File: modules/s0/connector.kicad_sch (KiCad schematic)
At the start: 15 parts, among them J1 P8, J2 P9, J3 USB_C_Receptacle_USB2.0_14P, J4 BAT_JST_01x02, U2 LM2575S-3.3(UMW), U4 BEAGLEBONEBLACK

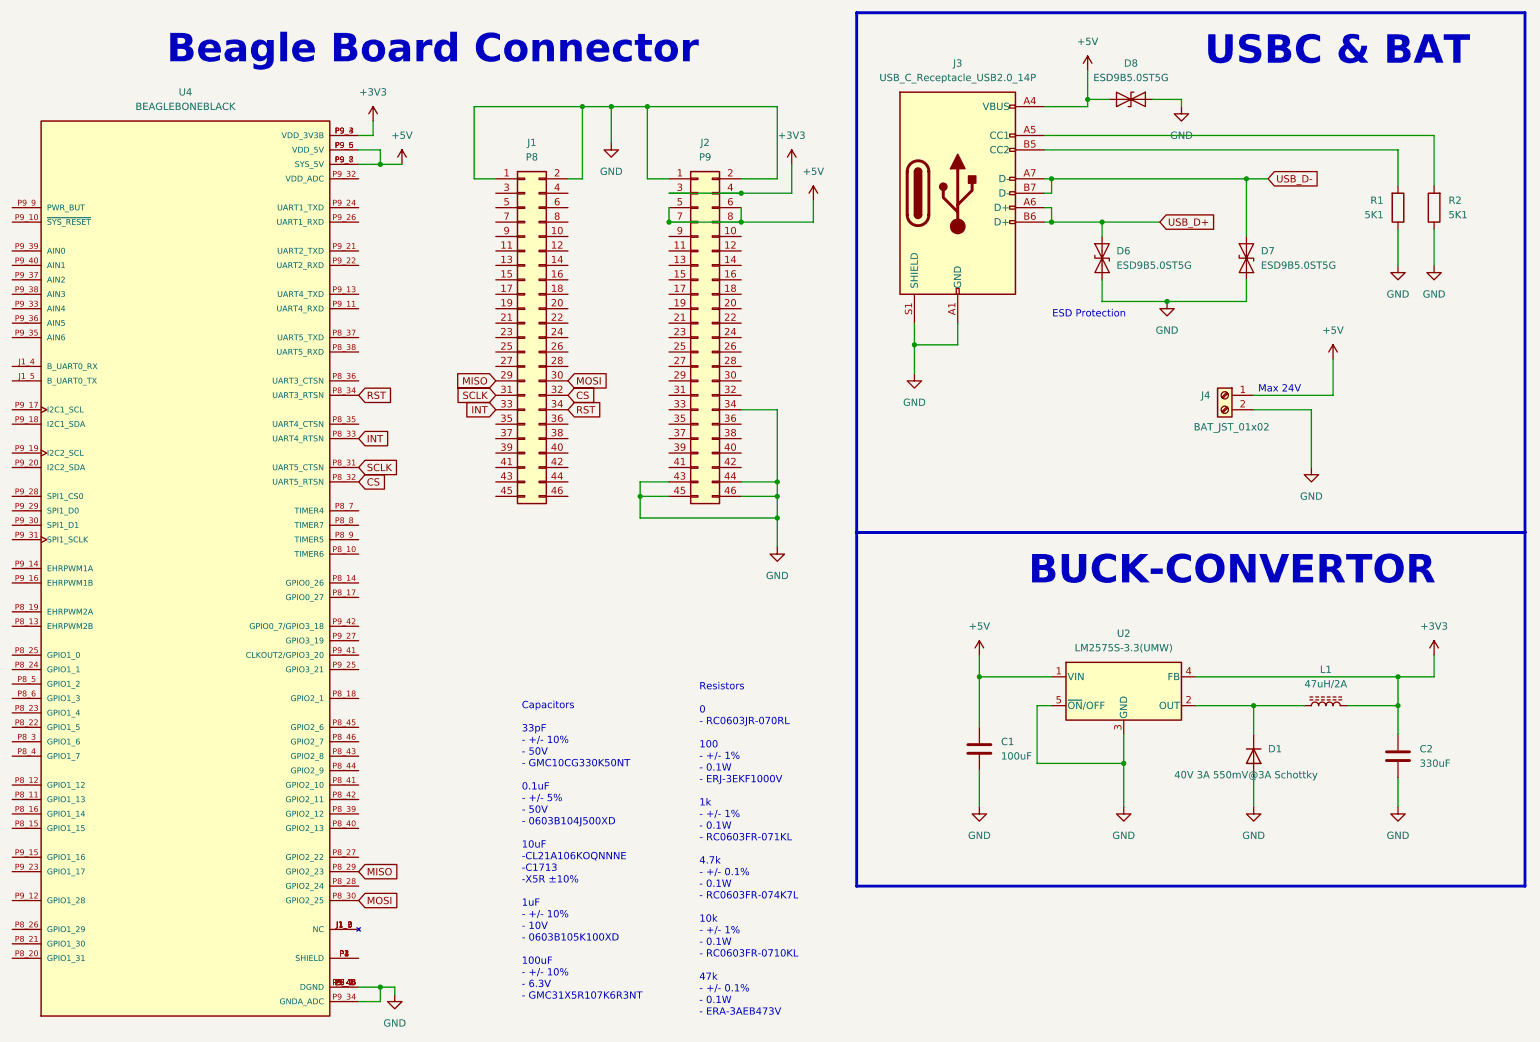
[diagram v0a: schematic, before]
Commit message: fix: add fuse, ferrite bead and fixes from gpt
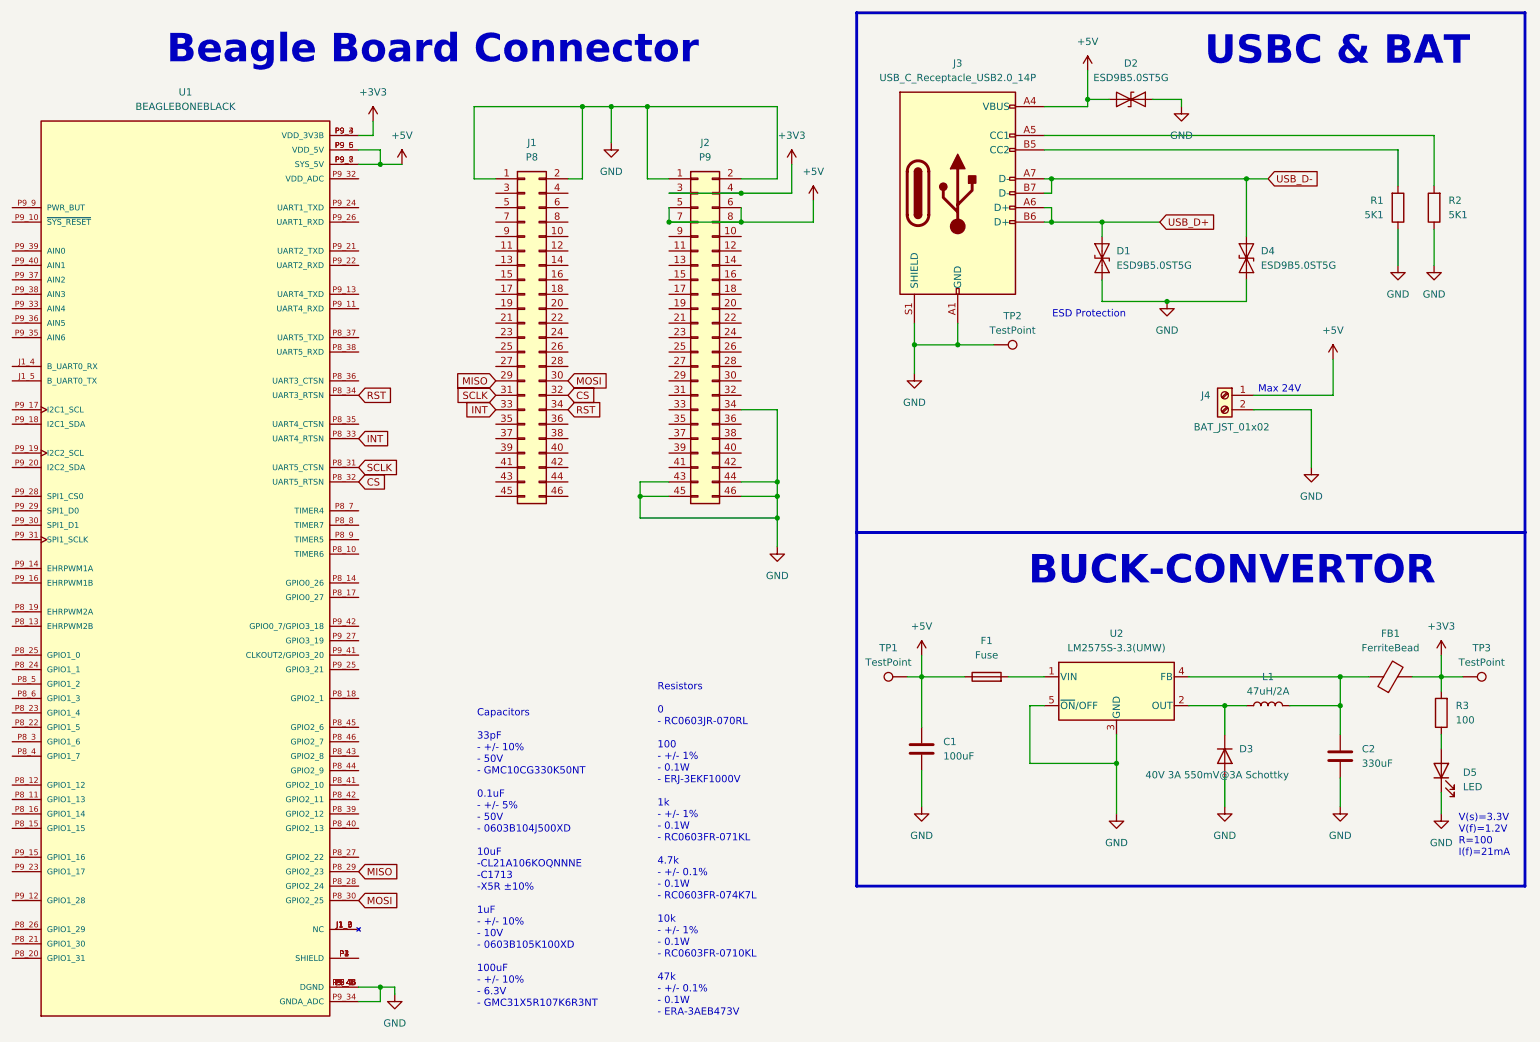
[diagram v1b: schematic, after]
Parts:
- added D5: LED, LED_SMD:LED_0603_1608Metric, symbol Device:LED
- added F1: Fuse, Fuse:Fuse_1206_3216Metric_Pad1.42x1.75mm_HandSolder, symbol Device:Fuse
- added FB1: FerriteBead, Inductor_SMD:L_1206_3216Metric_Pad1.22x1.90mm_HandSolder, symbol Device:FerriteBead
- added R3: 100, Resistor_SMD:R_0402_1005Metric, symbol Device:R
- added TP1, TP2, TP3: TestPoint, TestPoint:TestPoint_Pad_D1.0mm, symbol Connector:TestPoint
- L1: symbol Device:L_Ferrite -> Device:L
- renumbered D6 to D1, D8 to D2, D1 to D3, D7 to D4, U4 to U1
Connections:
- net +3V3: now also FB1.2, R3.2, TP3.1; no longer C2.1, L1.2, U2.4 (FB)
- net +5V: now also F1.1, TP1.1; no longer U2.1 (VIN)
- net GND: now also D5.1 (K), TP2.1
- new net: C2.1, FB1.1, L1.2, U2.4 (FB)
- new net: F1.2, U2.1 (VIN)
- new net: D5.2 (A), R3.1
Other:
- note added: "V(s)=3.3V V(f)=1.2V R=100 I(f)=21mA"
- moved on the sheet: C1, C2, D3, U2

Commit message: chore: finalize production files for s0
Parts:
- C1: value 100uF -> 10uF
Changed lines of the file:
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@@
 			)
 		)
-		(property "Value" "100uF"
+		(property "Value" "10uF"
 			(at 182.88 143.5099 0)
 			(effects

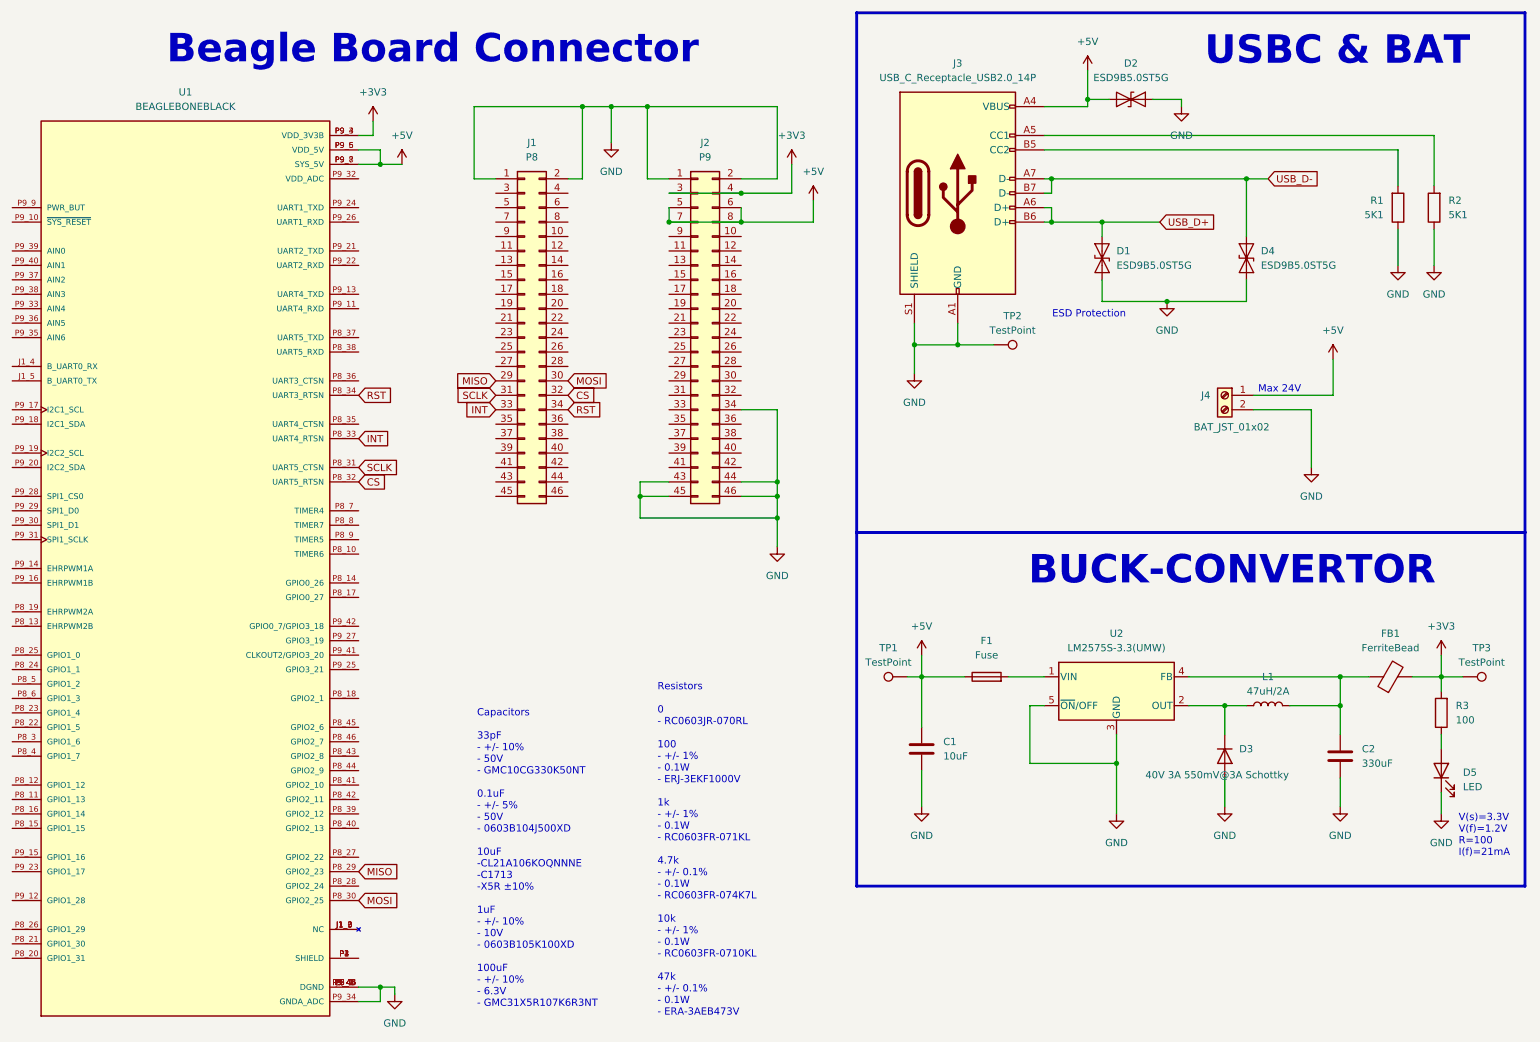
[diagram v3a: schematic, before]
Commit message: feat(s0): add GPIO mux for wired mbus and sd card
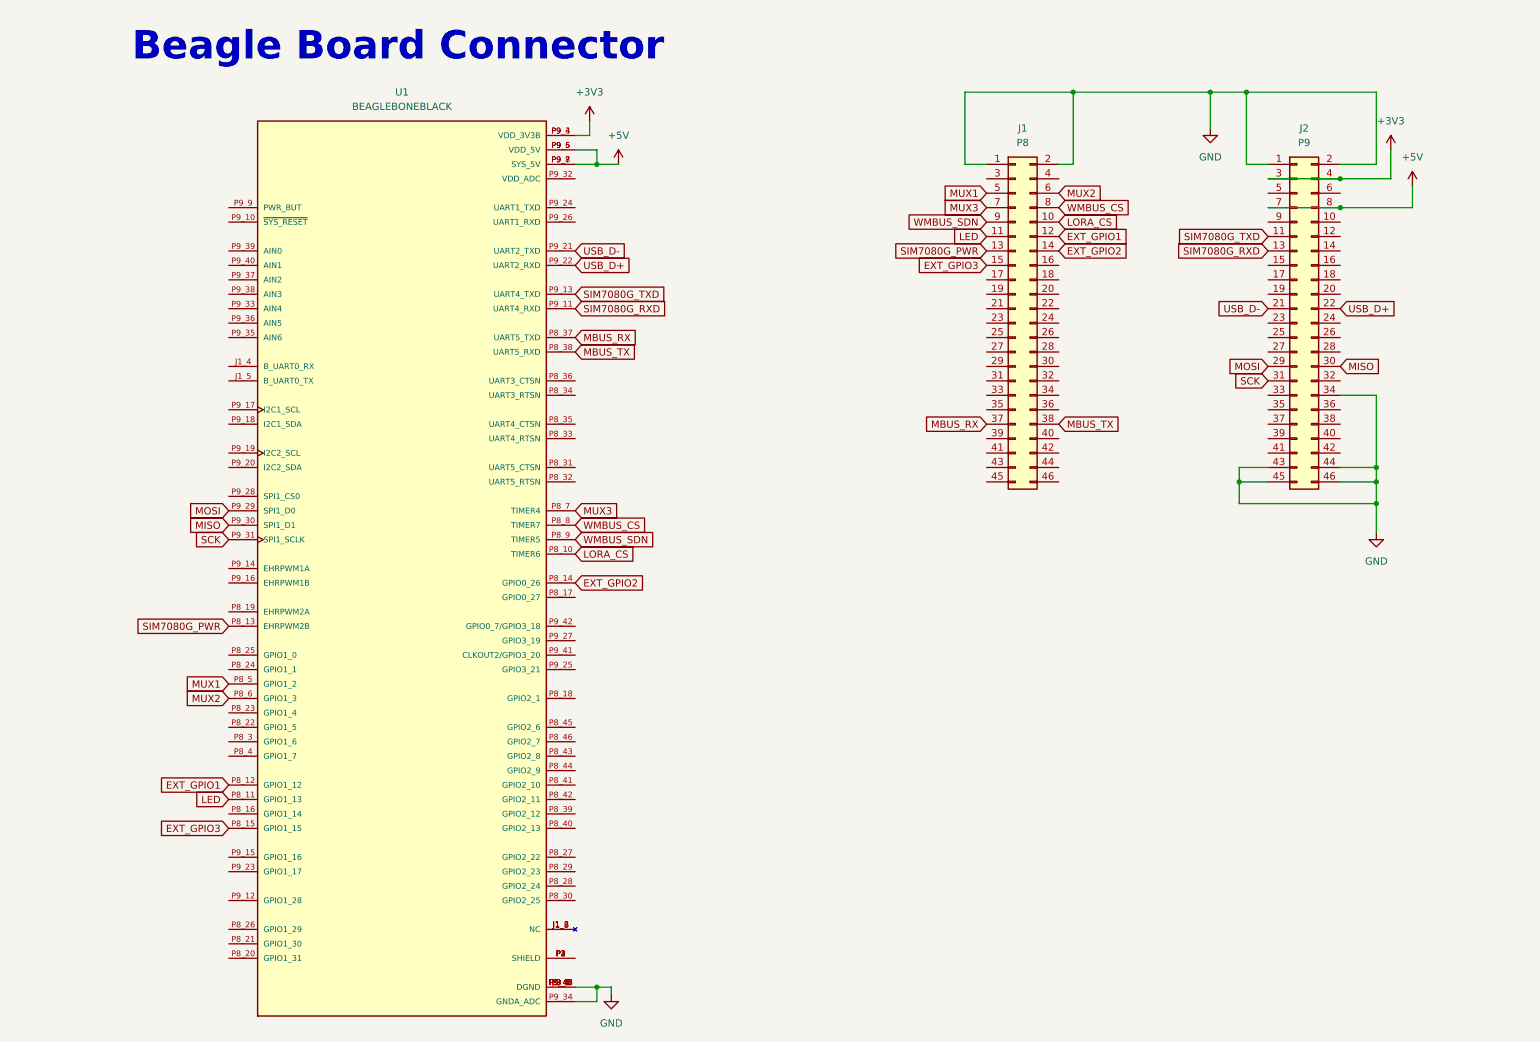
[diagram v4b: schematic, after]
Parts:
- removed C1: 10uF, Capacitor_SMD:C_0805_2012Metric, symbol Device:C
- removed C2: 330uF, Capacitor_SMD:C_0805_2012Metric, symbol Device:C
- removed D1, D2, D4: ESD9B5.0ST5G, Diode_SMD:D_SOD-923, symbol Diode:ESD9B5.0ST5G
- removed D3: 40V 3A 550mV@3A Schottky, Diode_SMD:D_SMA-SMB_Universal_Handsoldering, symbol Device:D
- removed D5: LED, LED_SMD:LED_0603_1608Metric, symbol Device:LED
- removed F1: Fuse, Fuse:Fuse_1206_3216Metric_Pad1.42x1.75mm_HandSolder, symbol Device:Fuse
- removed FB1: FerriteBead, Inductor_SMD:L_1206_3216Metric_Pad1.22x1.90mm_HandSolder, symbol Device:FerriteBead
- removed J3: USB_C_Receptacle_USB2.0_14P, Connector_USB:USB_C_Receptacle_G-Switch_GT-USB-7010ASV, symbol Connector:USB_C_Receptacle_USB2.0_14P
- removed J4: BAT_JST_01x02, Connector_JST:JST_EH_B2B-EH-A_1x02_P2.50mm_Vertical, symbol Connector:Screw_Terminal_01x02
- removed L1: 47uH/2A, Inductor_SMD:L_Chilisin_BMRB00060624, symbol Device:L
- removed R1, R2: 5K1, Resistor_SMD:R_0603_1608Metric, symbol Device:R
- removed R3: 100, Resistor_SMD:R_0402_1005Metric, symbol Device:R
- removed TP1, TP2, TP3: TestPoint, TestPoint:TestPoint_Pad_D1.0mm, symbol Connector:TestPoint
- removed U2: LM2575S-3.3(UMW), Package_TO_SOT_SMD:TO-263-5_TabPin3, symbol Regulator_Switching:LM2575-3.3BU
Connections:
- net +5V: no longer J2.5 (Pin_5), J2.6 (Pin_6)
- net MISO: now also J2.30 (Pin_30), U1.P9_30 (SPI1_D1); no longer J1.29 (Pin_29), U1.P8_29 (GPIO2_23)
- net MOSI: now also J2.29 (Pin_29), U1.P9_29 (SPI1_D0); no longer J1.30 (Pin_30), U1.P8_30 (GPIO2_25)
- net USB_D+: now also J2.22 (Pin_22), U1.P9_22 (UART2_RXD)
- net USB_D-: now also J2.21 (Pin_21), U1.P9_21 (UART2_TXD)
- net LORA_CS: now reaches U1.P8_10 (TIMER6)
- net LORA_CS: now also J1.10 (Pin_10)
- net LED: now reaches U1.P8_11 (GPIO1_13)
- net LED: now also J1.11 (Pin_11)
- net EXT_GPIO1: now reaches U1.P8_12 (GPIO1_12)
- net EXT_GPIO1: now also J1.12 (Pin_12)
- net SIM7080G_PWR: now reaches U1.P8_13 (EHRPWM2B)
- net SIM7080G_PWR: now also J1.13 (Pin_13)
- net EXT_GPIO2: now reaches U1.P8_14 (GPIO0_26)
- net EXT_GPIO2: now also J1.14 (Pin_14)
- net EXT_GPIO3: now reaches U1.P8_15 (GPIO1_15)
- net EXT_GPIO3: now also J1.15 (Pin_15)
- net MBUS_RX: now reaches U1.P8_37 (UART5_TXD)
- net MBUS_RX: now also J1.37 (Pin_37)
- net MBUS_TX: now reaches U1.P8_38 (UART5_RXD)
- net MBUS_TX: now also J1.38 (Pin_38)
- net MUX1: now reaches U1.P8_5 (GPIO1_2)
- net MUX1: now also J1.5 (Pin_5)
- net MUX2: now reaches U1.P8_6 (GPIO1_3)
- net MUX2: now also J1.6 (Pin_6)
- net MUX3: now reaches U1.P8_7 (TIMER4)
- net MUX3: now also J1.7 (Pin_7)
- net WMBUS_CS: now reaches U1.P8_8 (TIMER7)
- net WMBUS_CS: now also J1.8 (Pin_8)
- net WMBUS_SDN: now reaches U1.P8_9 (TIMER5)
- net WMBUS_SDN: now also J1.9 (Pin_9)
- net SIM7080G_RXD: now reaches U1.P9_11 (UART4_RXD)
- net SIM7080G_RXD: now also J2.13 (Pin_13)
- net SIM7080G_TXD: now reaches U1.P9_13 (UART4_TXD)
- net SIM7080G_TXD: now also J2.11 (Pin_11)
- net SCK: now reaches U1.P9_31 (SPI1_SCLK)
- net SCK: now also J2.31 (Pin_31)
- net CS: no longer names the net of U1.P8_32 (UART5_RTSN)
- net CS: no longer J1.32 (Pin_32)
- net INT: no longer names the net of U1.P8_33 (UART4_RTSN)
- net INT: no longer J1.33 (Pin_33)
- net RST: no longer names the net of U1.P8_34 (UART3_RTSN)
- net RST: no longer J1.34 (Pin_34)
- net SCLK: no longer names the net of U1.P8_31 (UART5_CTSN)
- net SCLK: no longer J1.31 (Pin_31)
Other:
- note removed: "BUCK-CONVERTOR"
- note removed: "Capacitors 33pF - +/- 10% - 50V - GMC10CG330K50NT 0.1uF - +/- 5% - 50V - 0603B104J500XD 10uF -CL21A106KOQNNNE -C1713 -X5R ±10% 1uF - +/- 10% - 10V - 0603B105K100XD 100uF - +/- 10% - 6.3V - GMC31X5R107K6R3NT"
- note removed: "ESD Protection"
- note removed: "Max 24V"
- note removed: "Resistors 0 - RC0603JR-070RL 100 - +/- 1% - 0.1W - ERJ-3EKF1000V 1k - +/- 1% - 0.1W - RC0603FR-071KL 4.7k - +/- 0.1% - 0.1W - RC0603FR-074K7L 10k - +/- 1% - 0.1W - RC0603FR-0710KL 47k - +/- 0.1% - 0.1W - ERA-3AEB473V"
- note removed: "USBC & BAT"
- note removed: "V(s)=3.3V V(f)=1.2V R=100 I(f)=21mA"
- moved on the sheet: J1, J2, U1

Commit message: fix: route PCB
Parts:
- U1: now left out of the parts list
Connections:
- net +5V: no longer U1.P9_5 (VDD_5V), U1.P9_6 (VDD_5V)
- new net: U1.P9_5 (VDD_5V), U1.P9_6 (VDD_5V)
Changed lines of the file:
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@@
-	)
-	(junction
-		(at 121.92 39.37)
-		(diameter 0)
-		(color 0 0 0 0)
 	)
 	(junction
@@
 	(wire
 		(pts
-			(xy 118.11 39.37) (xy 121.92 39.37)
+			(xy 118.11 39.37) (xy 125.73 39.37)
 		)
 		(stroke
@@
 	(wire
 		(pts
-			(xy 118.11 36.83) (xy 121.92 36.83)
-		)
-		(stroke
-			(width 0)
-			(type default)
-		)
-	)
-	(wire
-		(pts
 			(xy 234.95 95.25) (xy 240.03 95.25)
 		)
@@
 	(wire
 		(pts
-			(xy 121.92 36.83) (xy 121.92 39.37)
-		)
-		(stroke
-			(width 0)
-			(type default)
-		)
-	)
-	(wire
-		(pts
 			(xy 240.03 39.37) (xy 236.22 39.37)
 		)
@@
 		(pts
 			(xy 261.62 36.83) (xy 261.62 41.91)
-		)
-		(stroke
-			(width 0)
-			(type default)
-		)
-	)
-	(wire
-		(pts
-			(xy 121.92 39.37) (xy 125.73 39.37)
 		)
 		(stroke
@@
 		(unit 1)
 		(exclude_from_sim no)
-		(in_bom yes)
+		(in_bom no)
 		(on_board yes)
 		(dnp no)

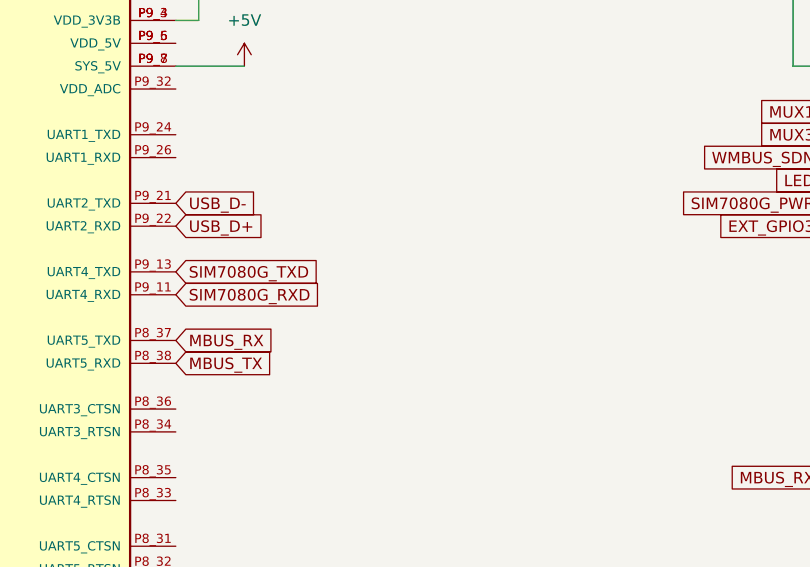
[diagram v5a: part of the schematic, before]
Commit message: fix: add UART switch for NBIoT and external connector for RS232 connector
Signed-off-by: Rodney Osodo <socials@rodneyosodo.com>
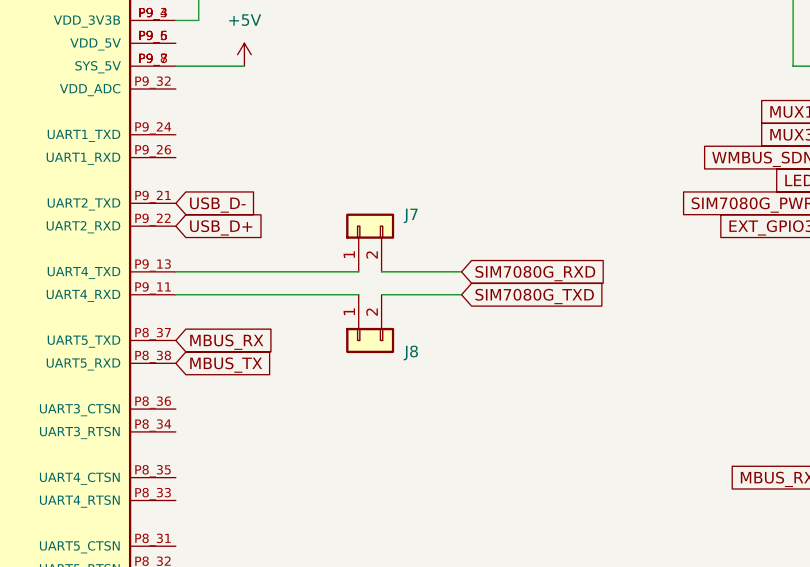
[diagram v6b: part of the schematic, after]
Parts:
- added J7, J8: Conn_01x02, Connector_PinHeader_2.54mm:PinHeader_1x02_P2.54mm_Vertical, symbol Connector_Generic:Conn_01x02
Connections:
- net SIM7080G_RXD: now also J7.2 (Pin_2); no longer U1.P9_11 (UART4_RXD)
- net SIM7080G_TXD: now also J8.2 (Pin_2); no longer U1.P9_13 (UART4_TXD)
- new net: J8.1 (Pin_1), U1.P9_11 (UART4_RXD)
- new net: J7.1 (Pin_1), U1.P9_13 (UART4_TXD)
